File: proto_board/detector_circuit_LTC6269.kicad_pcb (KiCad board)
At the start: 4 copper layers, 69.2 x 53.2 mm, 43 parts, among them J1 DET_CONN_PWR, J2 SIPM_CONN, J3 DET_CONN, U12 LTC6269, U13 LTC6269

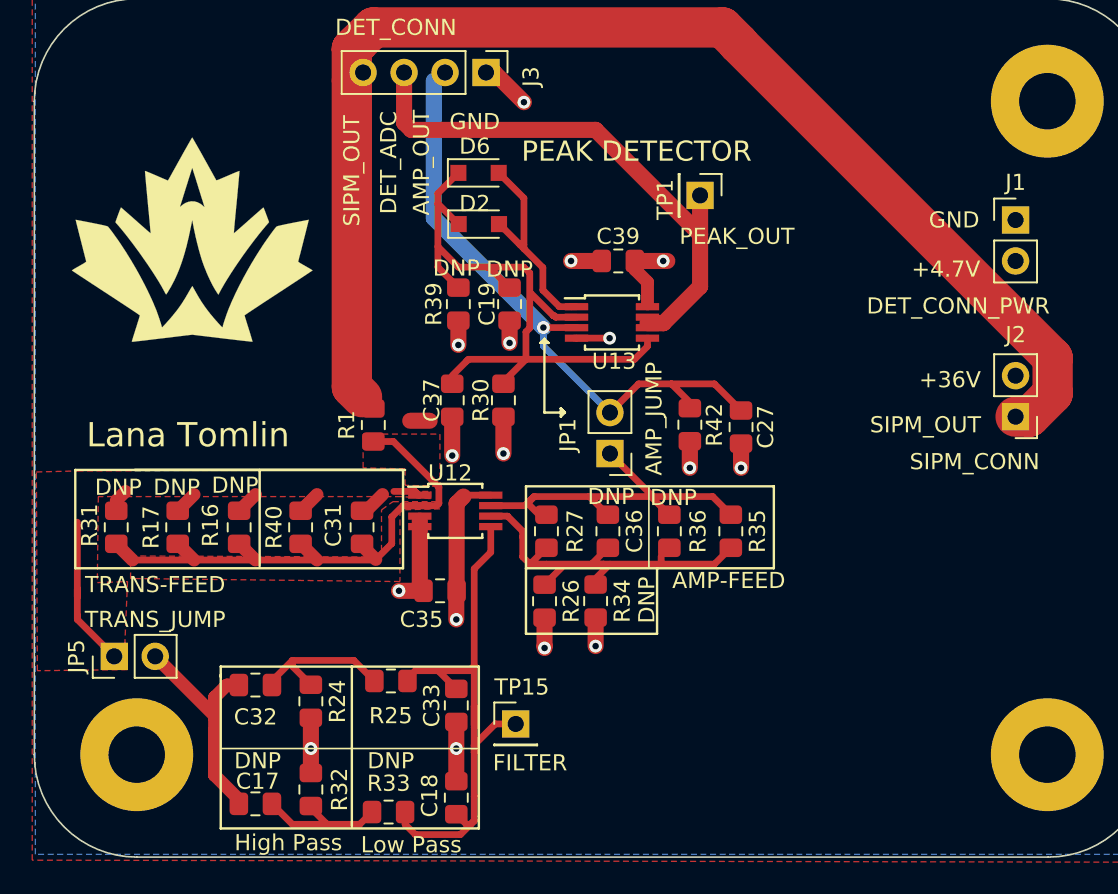
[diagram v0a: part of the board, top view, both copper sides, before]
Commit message: Fixedoverlapping copper areas & added name
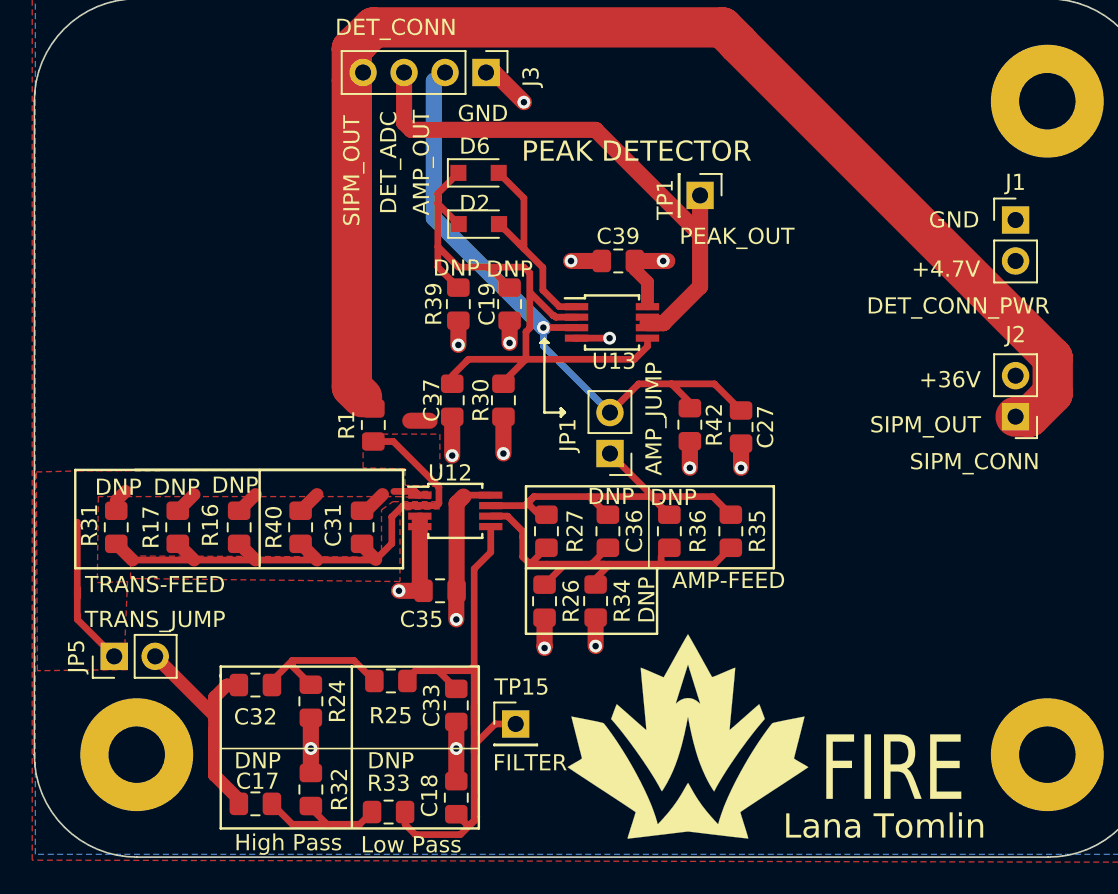
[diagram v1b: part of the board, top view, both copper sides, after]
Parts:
- moved G*** 43.5 mm to (124.3, 139.8)
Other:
- board text added: "FIRE"
